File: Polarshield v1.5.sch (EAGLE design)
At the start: 68 parts, among them CN1 1X4-CLEANBIG, CN2 1X4-CLEANBIG, J1 1X2-3.5MM, U1 ARDUINO_MEGA_SHIELD, X1 2.1MMJACKTHM

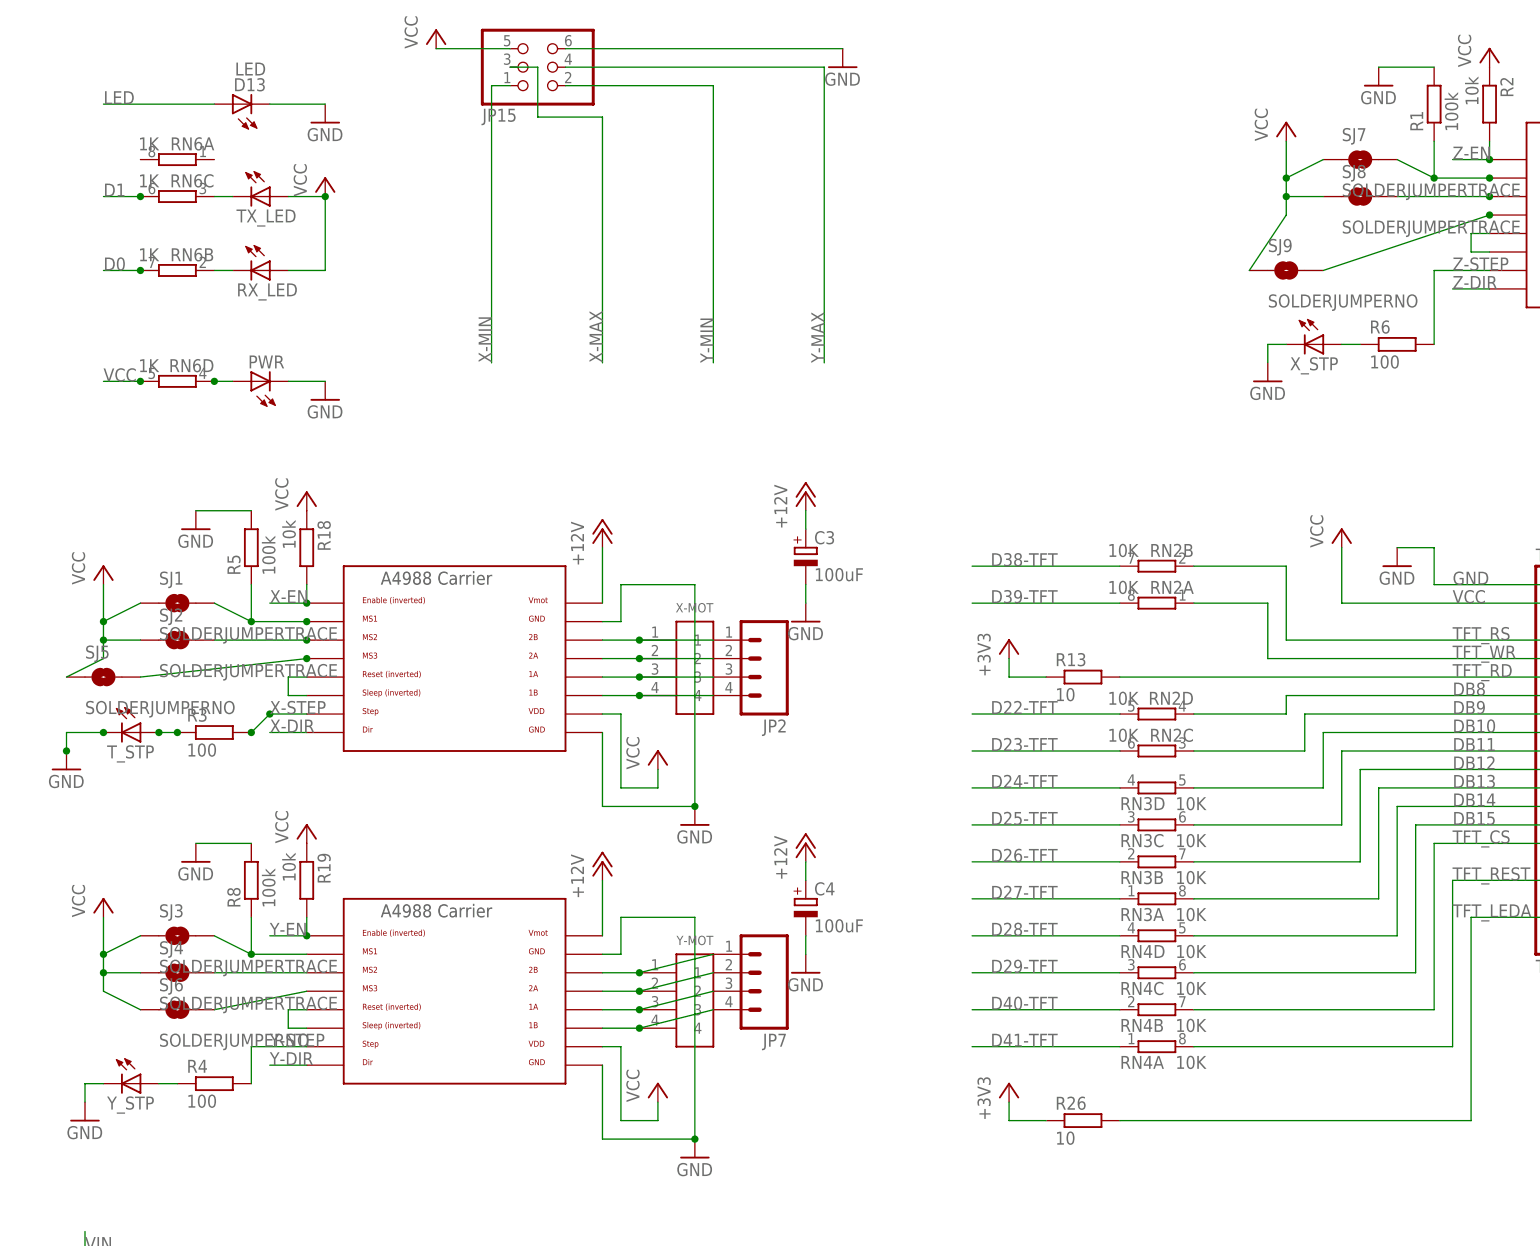
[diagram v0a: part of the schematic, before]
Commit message: Merged a resistor into a network and changed a few values, also cleaned up silkscreen.
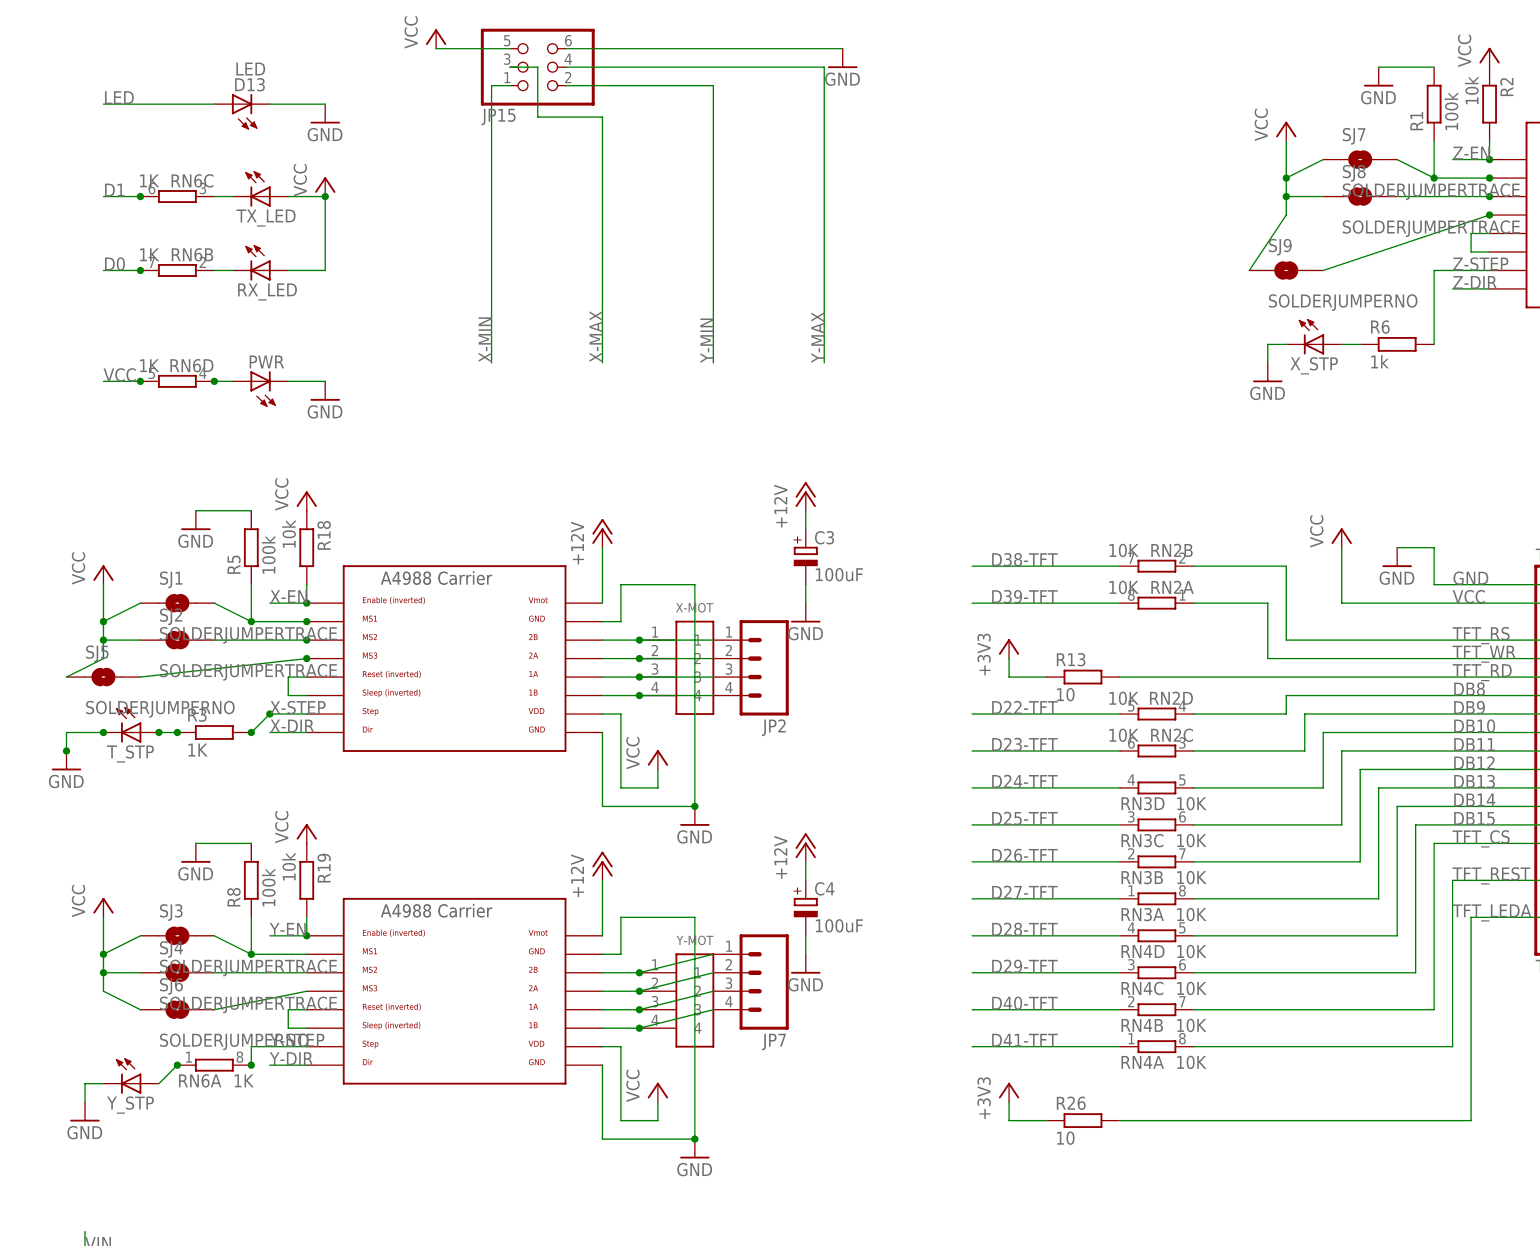
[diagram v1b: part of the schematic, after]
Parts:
- removed R4: 100, rcl:R-EU_R0805
- R3: value 100 -> 1K
- R6: value 100 -> 1k
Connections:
- net N$18: now also RN6A.1; no longer R4.1
- net Y-STEP: now also RN6A.2; no longer R4.2
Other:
- moved on the sheet: RN6A
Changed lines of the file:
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@@
 <part name="RN6" library="resistor-dil" deviceset="4R-N" device="EXBS8V" value="1K"/>
 <part name="T_STP" library="led" deviceset="LED" device="CHIP-LED0805"/>
-<part name="R3" library="rcl" deviceset="R-EU_" device="R0805" value="100"/>
+<part name="R3" library="rcl" deviceset="R-EU_" device="R0805" value="1K"/>
 <part name="GND12" library="supply1" deviceset="GND" device=""/>
 <part name="P+15" library="supply1" deviceset="VCC" device=""/>
-<part name="R4" library="rcl" deviceset="R-EU_" device="R0805" value="100"/>
 <part name="Y_STP" library="led" deviceset="LED" device="CHIP-LED0805"/>
 <part name="GND10" library="supply1" deviceset="GND" device=""/>
-<part name="R6" library="rcl" deviceset="R-EU_" device="R0805" value="100"/>
+<part name="R6" library="rcl" deviceset="R-EU_" device="R0805" value="1k"/>
 <part name="X_STP" library="led" deviceset="LED" device="CHIP-LED0805"/>
 <part name="GND11" library="supply1" deviceset="GND" device=""/>
@@
 <instance part="RN6" gate="B" x="0" y="53.34" rot="R180"/>
 <instance part="RN6" gate="C" x="0" y="63.5" rot="R180"/>
-<instance part="RN6" gate="A" x="0" y="68.58" rot="R180"/>
+<instance part="RN6" gate="A" x="5.08" y="-55.88"/>
 <instance part="T_STP" gate="G$1" x="-5.08" y="-10.16" rot="R270"/>
 <instance part="R3" gate="G$1" x="5.08" y="-10.16"/>
 <instance part="GND12" gate="1" x="-15.24" y="-15.24"/>
 <instance part="P+15" gate="VCC" x="20.32" y="66.04"/>
-<instance part="R4" gate="G$1" x="5.08" y="-58.42"/>
 <instance part="Y_STP" gate="G$1" x="-5.08" y="-58.42" rot="R270"/>
 <instance part="GND10" gate="1" x="-12.7" y="-63.5"/>
@@
 <label x="12.7" y="-53.34" size="1.778" layer="95"/>
 <pinref part="U$7" gate="G$1" pin="STEP"/>
-<pinref part="R4" gate="G$1" pin="2"/>
-<wire x1="10.16" y1="-53.34" x2="10.16" y2="-58.42" width="0.1524" layer="91"/>
+<wire x1="10.16" y1="-53.34" x2="10.16" y2="-55.88" width="0.1524" layer="91"/>
+<pinref part="RN6" gate="A" pin="2"/>
+<junction x="10.16" y="-55.88"/>
 </segment>
 <segment>
@@
 <net name="N$18" class="0">
 <segment>
-<pinref part="R4" gate="G$1" pin="1"/>
 <pinref part="Y_STP" gate="G$1" pin="A"/>
-<wire x1="0" y1="-58.42" x2="-2.54" y2="-58.42" width="0.1524" layer="91"/>
-</segment>
-</net>
+<wire x1="0" y1="-55.88" x2="-2.54" y2="-58.42" width="0.1524" layer="91"/>
+<pinref part="RN6" gate="A" pin="1"/>
+<junction x="0" y="-55.88"/>
+</segment>
+</net>
